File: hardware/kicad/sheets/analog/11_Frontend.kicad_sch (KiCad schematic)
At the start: 19 parts, among them Q16 L2N7002SLLT1G, SW8 DSHP04TS-S

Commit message: reorganized
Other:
- title: Frontend -> Analog Front-End
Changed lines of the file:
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@@
 	(paper "User" 297 210)
 	(title_block
-		(title "Frontend")
+		(title "Analog Front-End")
 		(date "2026-02-16")
 	)

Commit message: before final cleanup
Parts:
- renumbered 3V3 to 3V1, Q16 to Q11, R59 to R90, R290 to R91, R57 to R92, R294 to R93, R293 to R94, R292 to R95, R291 to R96, R336 to R97, R60 to R98, R181 to R99, SW8 to SW2

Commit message: imrpved footprints
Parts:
- BMSACTIVE1, BMSALERT1: footprint 5v rail sm-easyedapro:LED0603-RD_RED -> LED_SMD:LED_0603_1608Metric
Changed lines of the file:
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@@
 			)
 		)
-		(property "Footprint" "5v rail sm-easyedapro:LED0603-RD_RED"
+		(property "Footprint" "LED_SMD:LED_0603_1608Metric"
 			(at 68.58 53.34 0)
 			(effects
@@
 			)
 		)
-		(property "Footprint" "5v rail sm-easyedapro:LED0603-RD_RED"
+		(property "Footprint" "LED_SMD:LED_0603_1608Metric"
 			(at 146.05 38.1 0)
 			(effects

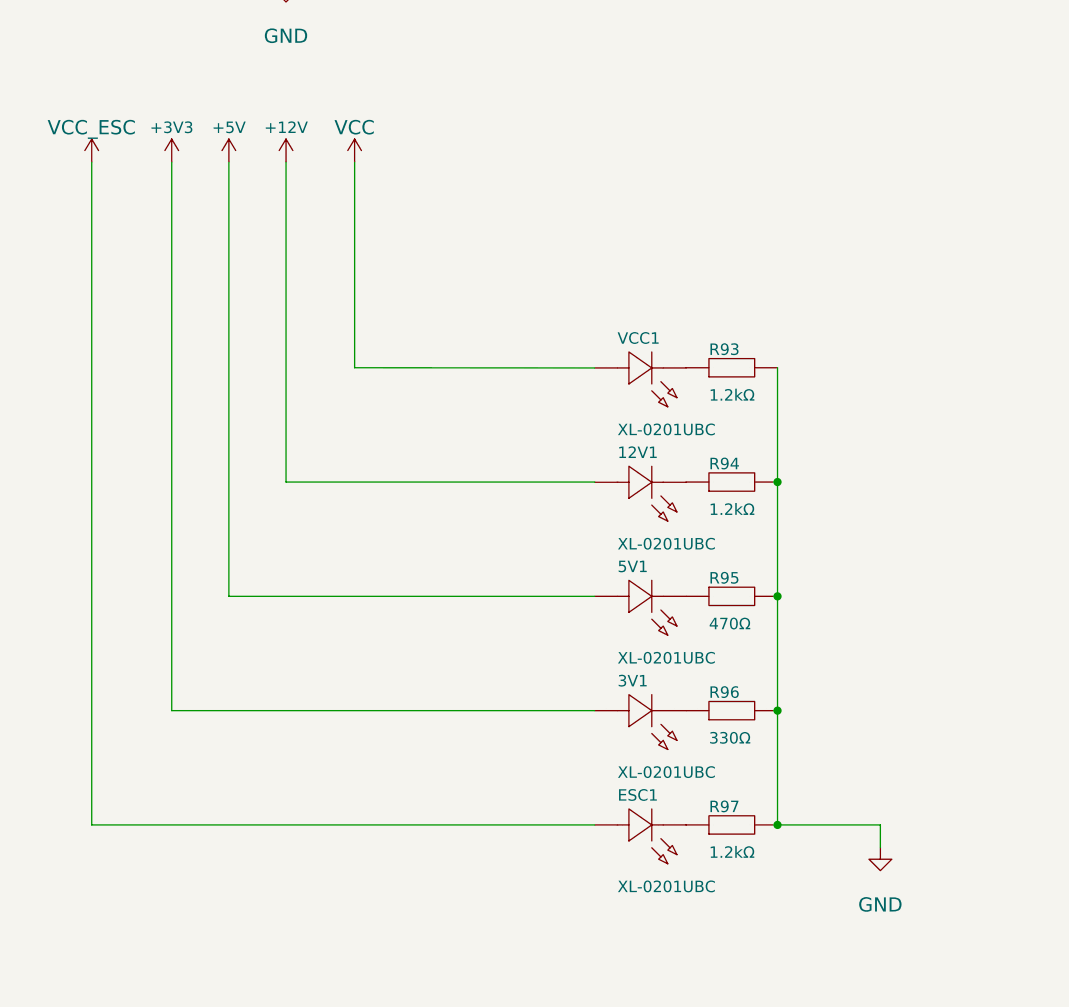
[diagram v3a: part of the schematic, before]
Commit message: better sheet nesting for power rails
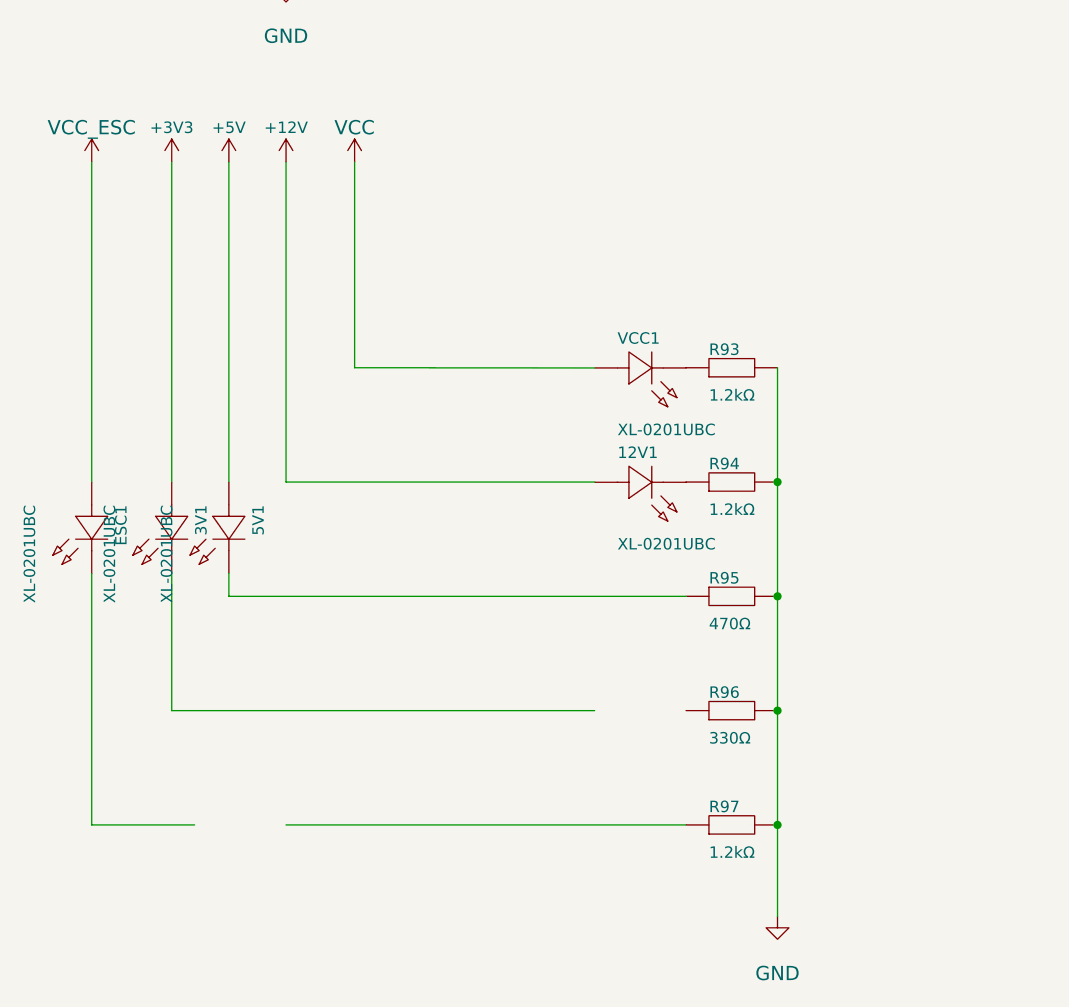
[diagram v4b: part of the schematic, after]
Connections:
- net at 3V1.1 (K): no longer R96.1
- net at ESC1.1 (K): no longer R97.1
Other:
- moved on the sheet: 3V1, 5V1, ESC1
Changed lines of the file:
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@@
+	(wire
+		(pts
+			(xy 46.99 152.4) (xy 46.99 180.34)
+		)
+		(stroke
+			(width 0)
+			(type default)
+		)
+	)
 	(wire
 		(pts
@@
 	(wire
 		(pts
-			(xy 134.62 180.34) (xy 123.19 180.34)
-		)
-		(stroke
-			(width 0)
-			(type default)
-		)
-	)
-	(wire
-		(pts
-			(xy 134.62 182.88) (xy 134.62 180.34)
+			(xy 123.19 190.5) (xy 123.19 180.34)
 		)
 		(stroke
@@
 	(wire
 		(pts
+			(xy 62.23 154.94) (xy 113.03 154.94)
+		)
+		(stroke
+			(width 0)
+			(type default)
+		)
+	)
+	(wire
+		(pts
 			(xy 83.82 69.85) (xy 80.01 69.85)
 		)
@@
 	(wire
 		(pts
-			(xy 62.23 106.68) (xy 62.23 154.94)
-		)
-		(stroke
-			(width 0)
-			(type default)
-		)
-	)
-	(wire
-		(pts
-			(xy 46.99 106.68) (xy 46.99 180.34)
-		)
-		(stroke
-			(width 0)
-			(type default)
-		)
-	)
-	(wire
-		(pts
-			(xy 62.23 154.94) (xy 102.87 154.94)
+			(xy 62.23 106.68) (xy 62.23 142.24)
+		)
+		(stroke
+			(width 0)
+			(type default)
+		)
+	)
+	(wire
+		(pts
+			(xy 46.99 106.68) (xy 46.99 142.24)
 		)
 		(stroke
@@
 	(wire
 		(pts
-			(xy 55.88 106.68) (xy 55.88 167.64)
+			(xy 55.88 106.68) (xy 55.88 142.24)
 		)
 		(stroke
@@
 	(wire
 		(pts
-			(xy 46.99 180.34) (xy 102.87 180.34)
+			(xy 68.58 180.34) (xy 113.03 180.34)
+		)
+		(stroke
+			(width 0)
+			(type default)
+		)
+	)
+	(wire
+		(pts
+			(xy 46.99 180.34) (xy 58.42 180.34)
 		)
 		(stroke
@@
 	(wire
 		(pts
+			(xy 55.88 152.4) (xy 55.88 167.64)
+		)
+		(stroke
+			(width 0)
+			(type default)
+		)
+	)
+	(wire
+		(pts
 			(xy 123.19 142.24) (xy 123.19 154.94)
 		)
@@
 		(pts
 			(xy 102.87 142.24) (xy 68.58 142.24)
+		)
+		(stroke
+			(width 0)
+			(type default)
+		)
+	)
+	(wire
+		(pts
+			(xy 62.23 152.4) (xy 62.23 154.94)
 		)
 		(stroke
@@
 	(symbol
 		(lib_id "5v rail sm-easyedapro:XL-0201UBC")
-		(at 107.95 154.94 180)
+		(at 62.23 147.32 90)
 		(unit 1)
 		(exclude_from_sim no)
@@
 		(dnp no)
 		(property "Reference" "5V1"
-			(at 105.41 152.4 0)
+			(at 64.77 144.78 0)
 			(effects
 				(font
@@
 		)
 		(property "Value" "XL-0201UBC"
-			(at 105.41 162.56 0)
+			(at 54.61 144.78 0)
 			(effects
 				(font
@@
 		)
 		(property "Footprint" "5v rail sm-easyedapro:LED-SMD_L0.7-W0.4-RD_BLUE"
-			(at 107.95 154.94 0)
+			(at 62.23 147.32 0)
 			(effects
 				(font
@@
 		)
 		(property "Datasheet" "https://atta.szlcsc.com/upload/public/pdf/source/20220704/BCF300BDAB27C0E3F48A6C7414571014.pdf"
-			(at 107.95 154.94 0)
+			(at 62.23 147.32 0)
 			(effects
 				(font
@@
 		)
 		(property "Description" "Emitted Color:Blue Forward Voltage (VF):2.6V~3.4V Forward Voltage (VF):2.6V~3.4V Power Dissipation:80mW Forward Current:5mA Dominant Wavelength:465nm~475nm Dominant Wavelength:465nm~475nm Lens Color:透明透镜 Luminous Intensity:40mcd~100mcd Luminous Intensity:"
-			(at 107.95 154.94 0)
+			(at 62.23 147.32 0)
 			(effects
 				(font
@@
 		)
 		(property "Manufacturer Part" "XL-0201UBC"
-			(at 107.95 154.94 0)
+			(at 62.23 147.32 0)
 			(effects
 				(font
@@
 		)
 		(property "Manufacturer" "XINGLIGHT(成兴光)"
-			(at 107.95 154.94 0)
+			(at 62.23 147.32 0)
 			(effects
 				(font
@@
 		)
 		(property "Supplier Part" "C3646921"
-			(at 107.95 154.94 0)
+			(at 62.23 147.32 0)
 			(effects
 				(font
@@
 		)
 		(property "Supplier" "LCSC"
-			(at 107.95 154.94 0)
+			(at 62.23 147.32 0)
 			(effects
 				(font
@@
 		)
 		(property "LCSC Part Name" "XL-0201UBC"
-			(at 107.95 154.94 0)
+			(at 62.23 147.32 0)
 			(effects
 				(font
@@
 	(symbol
 		(lib_id "5v rail sm-easyedapro:XL-0201UBC")
-		(at 107.95 167.64 180)
+		(at 55.88 147.32 90)
 		(unit 1)
 		(exclude_from_sim no)
@@
 		(dnp no)
 		(property "Reference" "3V1"
-			(at 105.41 165.1 0)
+			(at 58.42 144.78 0)
 			(effects
 				(font
@@
 		)
 		(property "Value" "XL-0201UBC"
-			(at 105.41 175.26 0)
+			(at 48.26 144.78 0)
 			(effects
 				(font
@@
 		)
 		(property "Footprint" "5v rail sm-easyedapro:LED-SMD_L0.7-W0.4-RD_BLUE"
-			(at 107.95 167.64 0)
+			(at 55.88 147.32 0)
 			(effects
 				(font
@@
 		)
 		(property "Datasheet" "https://atta.szlcsc.com/upload/public/pdf/source/20220704/BCF300BDAB27C0E3F48A6C7414571014.pdf"
-			(at 107.95 167.64 0)
+			(at 55.88 147.32 0)
 			(effects
 				(font
@@
 		)
 		(property "Description" "Emitted Color:Blue Forward Voltage (VF):2.6V~3.4V Forward Voltage (VF):2.6V~3.4V Power Dissipation:80mW Forward Current:5mA Dominant Wavelength:465nm~475nm Dominant Wavelength:465nm~475nm Lens Color:透明透镜 Luminous Intensity:40mcd~100mcd Luminous Intensity:"
-			(at 107.95 167.64 0)
+			(at 55.88 147.32 0)
 			(effects
 				(font
@@
 		)
 		(property "Manufacturer Part" "XL-0201UBC"
-			(at 107.95 167.64 0)
+			(at 55.88 147.32 0)
 			(effects
 				(font
@@
 		)
 		(property "Manufacturer" "XINGLIGHT(成兴光)"
-			(at 107.95 167.64 0)
+			(at 55.88 147.32 0)
 			(effects
 				(font
@@
 		)
 		(property "Supplier Part" "C3646921"
-			(at 107.95 167.64 0)
+			(at 55.88 147.32 0)
 			(effects
 				(font
@@
 		)
 		(property "Supplier" "LCSC"
-			(at 107.95 167.64 0)
+			(at 55.88 147.32 0)
 			(effects
 				(font
@@
 		)
 		(property "LCSC Part Name" "XL-0201UBC"
-			(at 107.95 167.64 0)
+			(at 55.88 147.32 0)
 			(effects
 				(font
@@
 	(symbol
 		(lib_id "5v rail sm-easyedapro:XL-0201UBC")
-		(at 107.95 180.34 180)
+		(at 46.99 147.32 90)
 		(unit 1)
 		(exclude_from_sim no)
@@
 		(dnp no)
 		(property "Reference" "ESC1"
-			(at 105.41 177.8 0)
+			(at 49.53 144.78 0)
 			(effects
 				(font
@@
 		)
 		(property "Value" "XL-0201UBC"
-			(at 105.41 187.96 0)
+			(at 39.37 144.78 0)
 			(effects
 				(font
@@
 		)
 		(property "Footprint" "5v rail sm-easyedapro:LED-SMD_L0.7-W0.4-RD_BLUE"
-			(at 107.95 180.34 0)
+			(at 46.99 147.32 0)
 			(effects
 				(font
@@
 		)
 		(property "Datasheet" "https://atta.szlcsc.com/upload/public/pdf/source/20220704/BCF300BDAB27C0E3F48A6C7414571014.pdf"
-			(at 107.95 180.34 0)
+			(at 46.99 147.32 0)
 			(effects
 				(font
@@
 		)
 		(property "Description" "Emitted Color:Blue Forward Voltage (VF):2.6V~3.4V Forward Voltage (VF):2.6V~3.4V Power Dissipation:80mW Forward Current:5mA Dominant Wavelength:465nm~475nm Dominant Wavelength:465nm~475nm Lens Color:透明透镜 Luminous Intensity:40mcd~100mcd Luminous Intensity:"
-			(at 107.95 180.34 0)
+			(at 46.99 147.32 0)
 			(effects
 				(font
@@
 		)
 		(property "Manufacturer Part" "XL-0201UBC"
-			(at 107.95 180.34 0)
+			(at 46.99 147.32 0)
 			(effects
 				(font
@@
 		)
 		(property "Manufacturer" "XINGLIGHT(成兴光)"
-			(at 107.95 180.34 0)
+			(at 46.99 147.32 0)
 			(effects
 				(font
@@
 		)
 		(property "Supplier Part" "C3646921"
-			(at 107.95 180.34 0)
+			(at 46.99 147.32 0)
 			(effects
 				(font
@@
 		)
 		(property "Supplier" "LCSC"
-			(at 107.95 180.34 0)
+			(at 46.99 147.32 0)
 			(effects
 				(font
@@
 		)
 		(property "LCSC Part Name" "XL-0201UBC"
-			(at 107.95 180.34 0)
+			(at 46.99 147.32 0)
 			(effects
 				(font
@@
 	(symbol
 		(lib_id "power:GND")
-		(at 134.62 182.88 0)
+		(at 123.19 190.5 0)
 		(unit 1)
 		(exclude_from_sim no)
@@
 		(dnp no)
 		(property "Reference" "#PWR0168"
-			(at 134.62 182.88 0)
+			(at 123.19 190.5 0)
 			(effects
 				(font
@@
 		)
 		(property "Value" "GND"
-			(at 134.62 189.23 0)
+			(at 123.19 196.85 0)
 			(effects
 				(font
@@
 		)
 		(property "Footprint" ""
-			(at 134.62 182.88 0)
+			(at 123.19 190.5 0)
 			(effects
 				(font
@@
 		)
 		(property "Datasheet" ""
-			(at 134.62 182.88 0)
+			(at 123.19 190.5 0)
 			(effects
 				(font
@@
 		)
 		(property "Description" ""
-			(at 134.62 182.88 0)
-			(effects
-				(font
+			(at 123.19 190.5 0)
+			(effects
+				(font

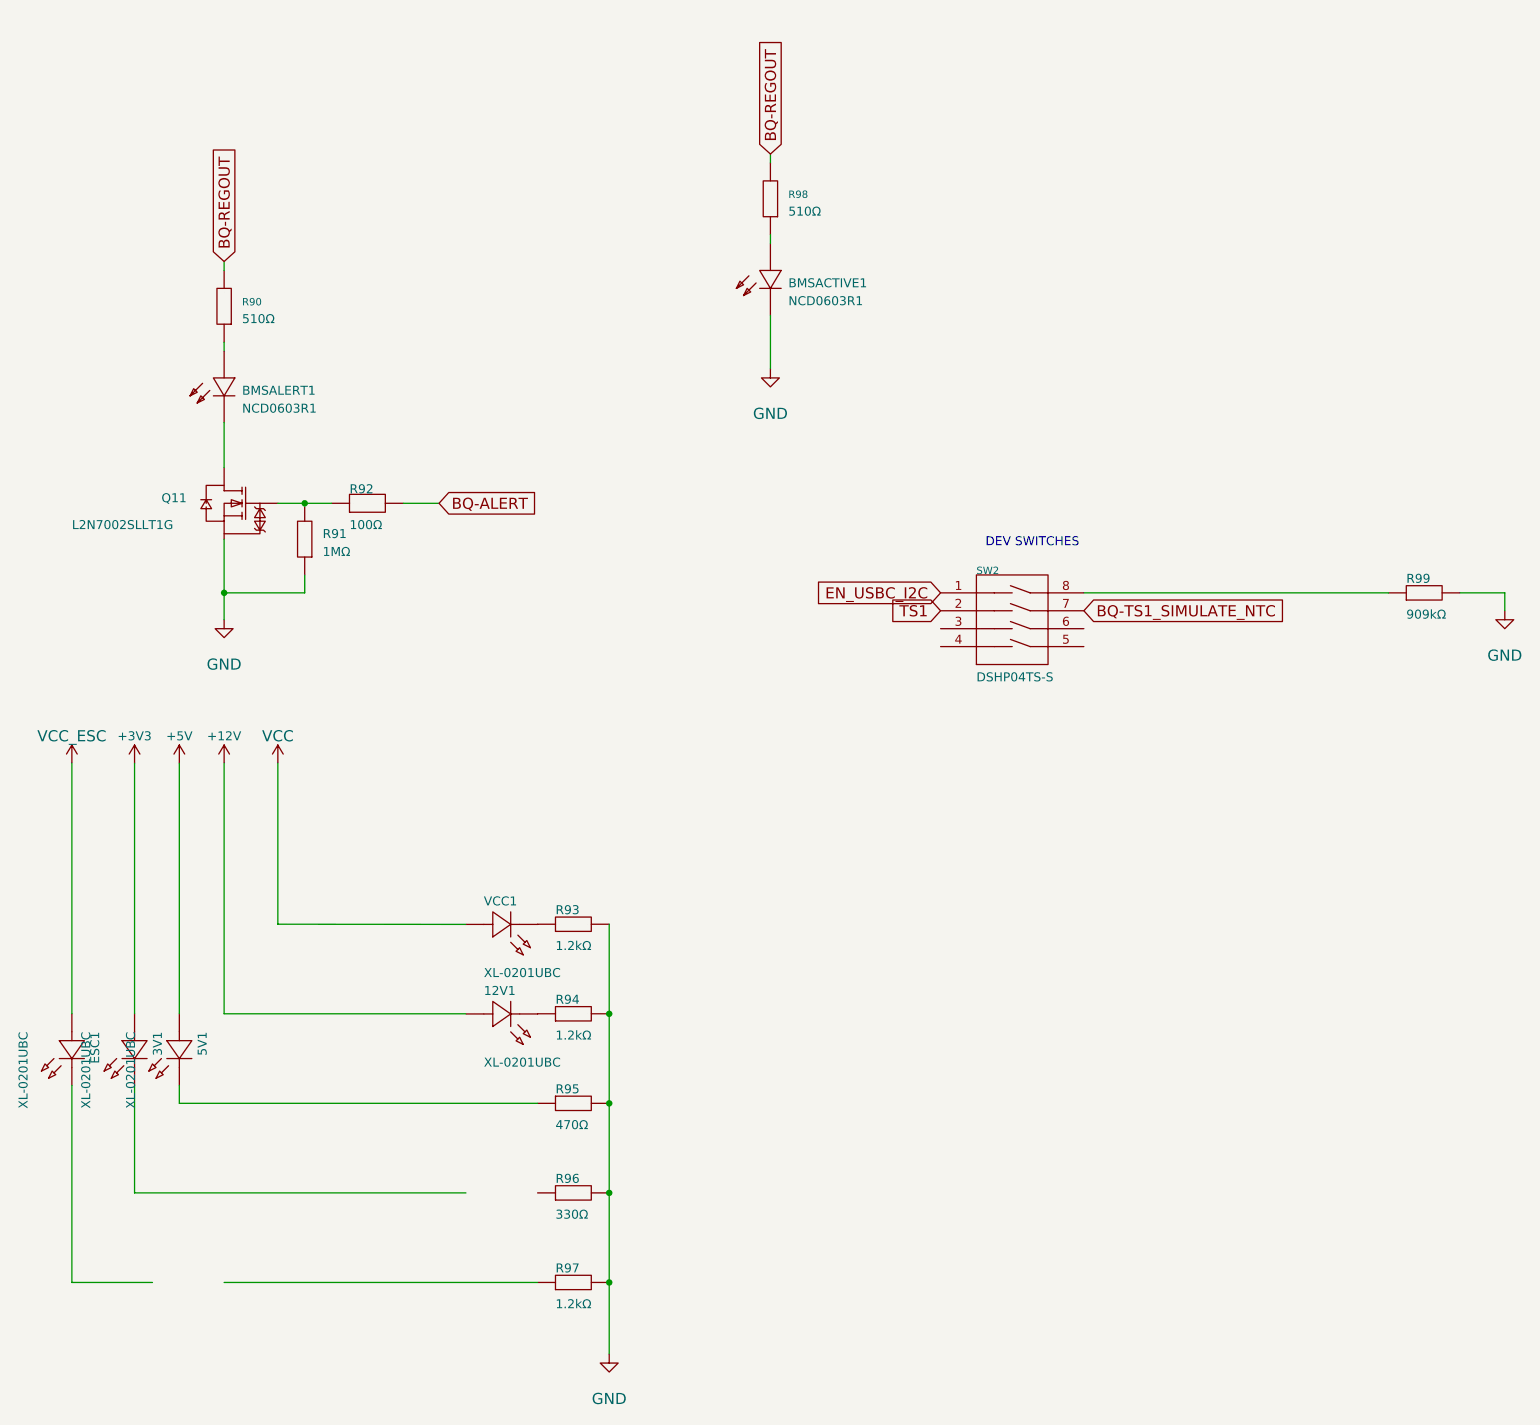
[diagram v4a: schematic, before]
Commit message: more sheet simplfiication and pre simpler 12v sym
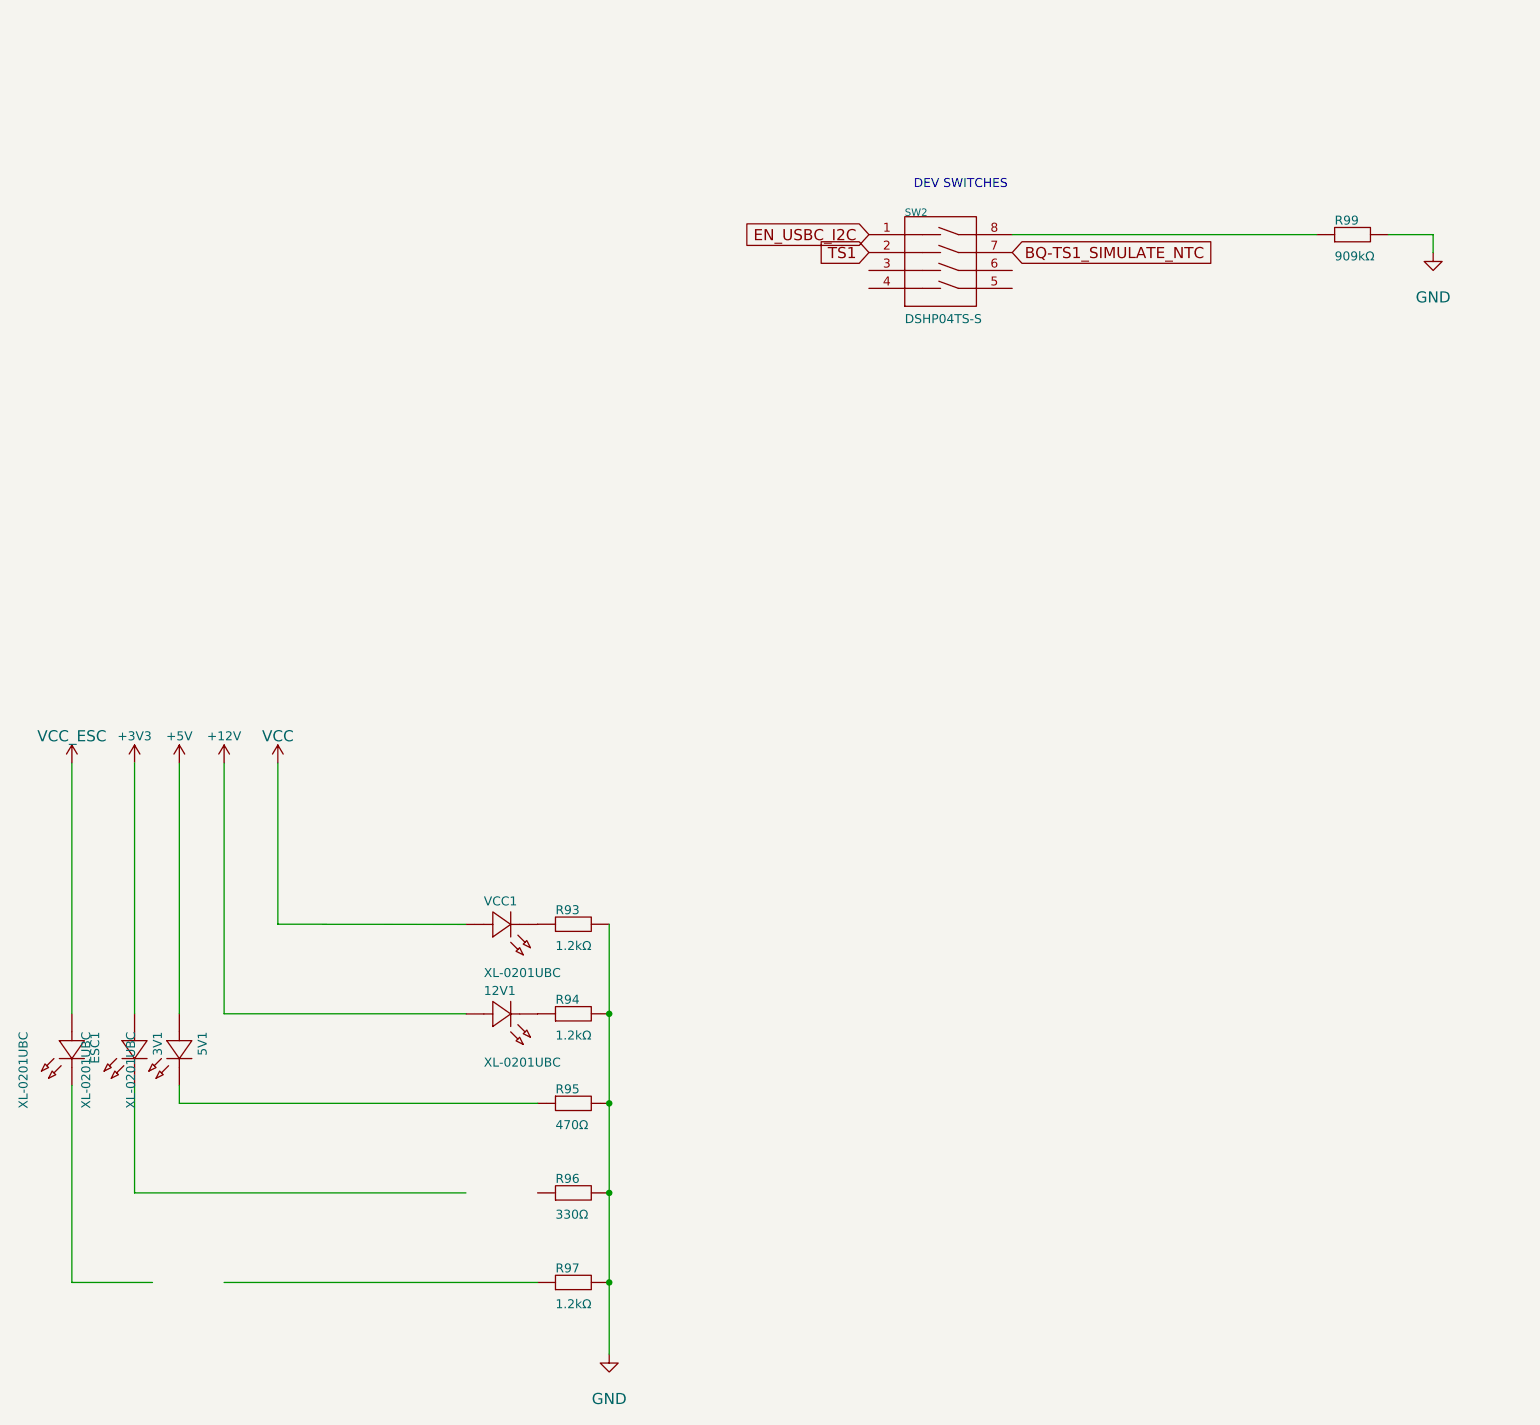
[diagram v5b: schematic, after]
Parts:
- removed BMSACTIVE1, BMSALERT1: NCD0603R1, LED_SMD:LED_0603_1608Metric, symbol 5v rail sm-easyedapro:FC-DA1608HRK-620D
- removed Q11: L2N7002SLLT1G, Package_TO_SOT_SMD:SOT-23, symbol 5v rail sm-easyedapro:L2N7002SLLT1G
- removed R90, R98: 510Ω, Resistor_SMD:R_0402_1005Metric, symbol 5v rail sm-easyedapro:0402WGF5100TCE
- removed R91: 1MΩ, Resistor_SMD:R_0201_0603Metric, symbol 5v rail sm-easyedapro:RC0201FR-071ML
- removed R92: 100Ω, Resistor_SMD:R_0402_1005Metric, symbol 5v rail sm-easyedapro:FRC0402F1000TS
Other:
- moved on the sheet: R99, SW2
